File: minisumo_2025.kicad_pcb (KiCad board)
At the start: 4 copper layers, 62.4 x 98 mm, 131 parts, among them J1 USB_C Connector, J10 DISTANCE_R90, J11 DISTANCE_R, J12 DISTANCE_RF, J13 DISTANCE_L90, J14 DISTANCE_L, J15 LINE_LEFT, J16 DISTANCE_LF, J3 START_MODULE, J4 MOTOR1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

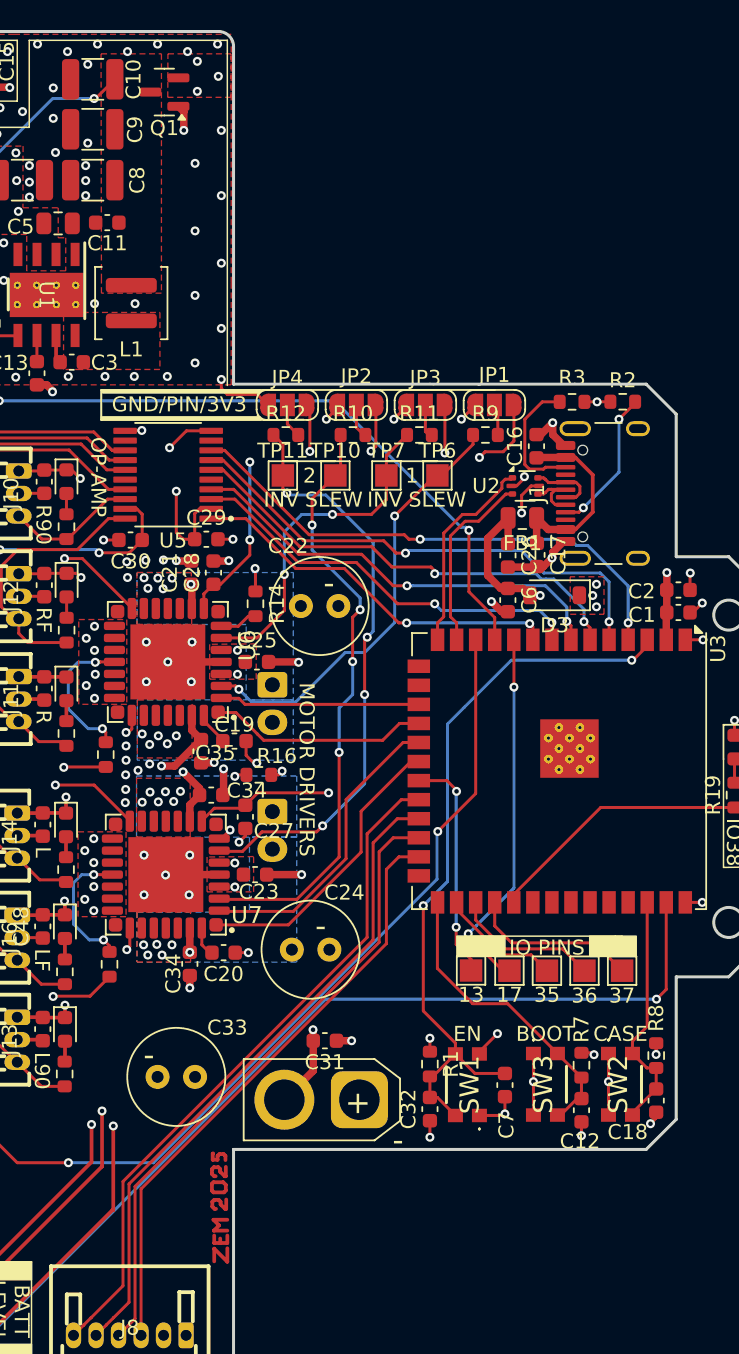
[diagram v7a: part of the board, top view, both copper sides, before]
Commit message: added global labels
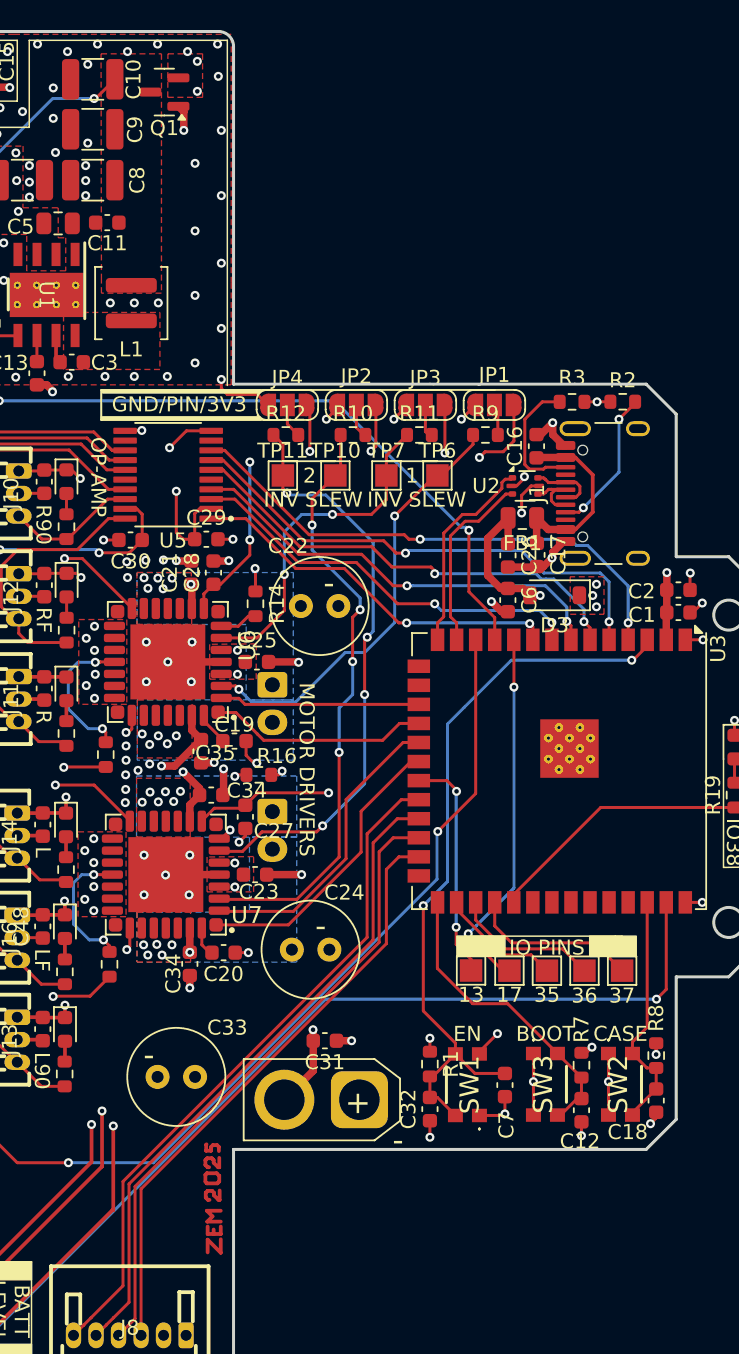
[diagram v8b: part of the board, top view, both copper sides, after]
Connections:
- net /CCP_1 renamed /DRIVERS/CCP_1
- net /CCP_2 renamed /DRIVERS/CCP_2
- net /DISTANCE_L90_OUT renamed /SENSORS/DISTANCE_L90_OUT
- net /DISTANCE_LF_OUT renamed /SENSORS/DISTANCE_LF_OUT
- net /DISTANCE_L_OUT renamed /SENSORS/DISTANCE_L_OUT
- net /DISTANCE_R90_OUT renamed /SENSORS/DISTANCE_R90_OUT
- net /DISTANCE_RF_OUT renamed /SENSORS/DISTANCE_RF_OUT
- net /DISTANCE_R_OUT renamed /SENSORS/DISTANCE_R_OUT
- net /D_N renamed /POWER/D_N
- net /D_P renamed /POWER/D_P
- net /ESP32/ESP_BOOT renamed ESP_BOOT
- net /ESP32/ESP_EN renamed ESP_EN
- net /INV_1 renamed /DRIVERS/INV_1
- net /INV_2 renamed /DRIVERS/INV_2
- net /LINE_LEFT_OUT renamed /SENSORS/LINE_LEFT_OUT
- net /LINE_RIGHT_OUT renamed /SENSORS/LINE_RIGHT_OUT
- net /MOTOR1_A renamed /DRIVERS/MOTOR1_A
- net /MOTOR1_B renamed /DRIVERS/MOTOR1_B
- net /MOTOR2_A renamed /DRIVERS/MOTOR2_A
- net /MOTOR2_B renamed /DRIVERS/MOTOR2_B
- net /SLEW_1 renamed /DRIVERS/SLEW_1
- net /SLEW_2 renamed /DRIVERS/SLEW_2
- net /VBUS renamed /POWER/VBUS
- C18 pad 1: /ESP32/CASE -> CASE
- J3 pad 3: /GPIO1 -> GPIO1
- J8 pad 3: /GPIO48 -> GPIO48
- J8 pad 4: /GPIO47 -> GPIO47
- J8 pad 5: /GPIO21 -> GPIO21
- J8 pad 6: /DISTANCE_INTR -> DISTANCE_INTR
- R19 pad 1: /GPIO38 -> GPIO38
- R21 pad 1: /GPIO18 -> GPIO18
- R22 pad 2: /GPIO18 -> GPIO18
- R23 pad 1: /GPIO8 -> GPIO8
- R24 pad 2: /GPIO8 -> GPIO8
- R8 pad 2: /ESP32/CASE -> CASE
- SW2 pad 2: /ESP32/CASE -> CASE
- SW2 pad 3: /ESP32/CASE -> CASE
- TP1 pad 1: /GPIO13 -> GPIO13
- TP12 pad 1: /GPIO37 -> GPIO37
- TP13 pad 1: /GPIO17 -> GPIO17
- TP8 pad 1: /GPIO35 -> GPIO35
- TP9 pad 1: /GPIO36 -> GPIO36
- U1 pad V: (no net) -> GND
- U2 pad 1: /D+ -> D+
- U2 pad 3: /D- -> D-
- U3 pad 10: /ESP32/GPIO17 -> GPIO17
- U3 pad 11: /ESP32/GPIO18 -> GPIO18
- U3 pad 12: /ESP32/GPIO8 -> GPIO8
- U3 pad 13: /ESP32/D- -> D-
- U3 pad 14: /ESP32/D+ -> D+
- U3 pad 17: /ESP32/GPIO9 -> GPIO9
- U3 pad 18: /ESP32/GPIO10 -> GPIO10
- U3 pad 19: /ESP32/GPIO11 -> GPIO11
- U3 pad 20: /ESP32/GPIO12 -> GPIO12
- U3 pad 21: /ESP32/GPIO13 -> GPIO13
- U3 pad 22: /ESP32/GPIO14 -> DISTANCE_INTR
- U3 pad 23: /ESP32/GPIO21 -> GPIO21
- U3 pad 24: /ESP32/GPIO47 -> GPIO47
- U3 pad 25: /ESP32/GPIO48 -> GPIO48
- U3 pad 28: /ESP32/GPIO35 -> GPIO35
- U3 pad 29: /ESP32/GPIO36 -> GPIO36
- U3 pad 30: /ESP32/GPIO37 -> GPIO37
- U3 pad 31: /ESP32/GPIO38 -> GPIO38
- U3 pad 38: /ESP32/GPIO2 -> CASE
- U3 pad 39: /ESP32/GPIO1 -> GPIO1
- U3 pad 4: /ESP32/GPIO4 -> DISTANCE_L90
- U3 pad 5: /ESP32/GPIO5 -> DISTANCE_LF
- U3 pad 6: /ESP32/GPIO6 -> DISTANCE_L
- U3 pad 7: /ESP32/GPIO7 -> DISTANCE_R
- U3 pad 8: /ESP32/GPIO15 -> DISTANCE_R90
- U3 pad 9: /ESP32/GPIO16 -> DISTANCE_RF
- U5 pad 1: /DISTANCE_RF -> DISTANCE_RF
- U5 pad 3: /DISTANCE_R90 -> DISTANCE_R90
- U5 pad 4: /DISTANCE_R -> DISTANCE_R
- U5 pad 6: /DISTANCE_L -> DISTANCE_L
- U5 pad 7: /DISTANCE_LF -> DISTANCE_LF
- U5 pad 8: /DISTANCE_L90 -> DISTANCE_L90
- U6 pad 1: /GPIO10 -> GPIO10
- U6 pad 2: /GPIO9 -> GPIO9
- U7 pad 1: /GPIO12 -> GPIO12
- U7 pad 2: /GPIO11 -> GPIO11
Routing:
- net GPIO1: track 0.00 -> 70.6 mm, vias 0 -> 1
- net /GPIO1: track 70.6 -> 0.00 mm, vias 1 -> 0
- net GPIO8: track 0.00 -> 65.4 mm, vias 0 -> 2
- net /GPIO8: track 65.4 -> 0.00 mm, vias 2 -> 0
- net GPIO18: track 0.00 -> 52.8 mm, vias 0 -> 2
- net /GPIO18: track 52.8 -> 0.00 mm, vias 2 -> 0
- net DISTANCE_INTR: track 0.00 -> 45.9 mm
- net /DISTANCE_INTR: track 45.9 -> 0.00 mm
- net GPIO21: track 0.00 -> 44.2 mm
- net /GPIO21: track 44.2 -> 0.00 mm
- net GPIO47: track 0.00 -> 42.4 mm
- net /GPIO47: track 42.4 -> 0.00 mm
- net GPIO48: track 0.00 -> 40.3 mm
- net /GPIO48: track 40.3 -> 0.00 mm
- net DISTANCE_L90: track 0.00 -> 35.1 mm, vias 0 -> 2
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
